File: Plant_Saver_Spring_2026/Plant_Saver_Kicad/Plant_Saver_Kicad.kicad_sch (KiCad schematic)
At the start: 27 parts, among them SW1 Up, SW2 Down, SW3 Change Screen, SW4 Select, U3 ESP32-WROOM-32D, U5 TPB4056A20-ES1R, U6 AMS1117-3.3

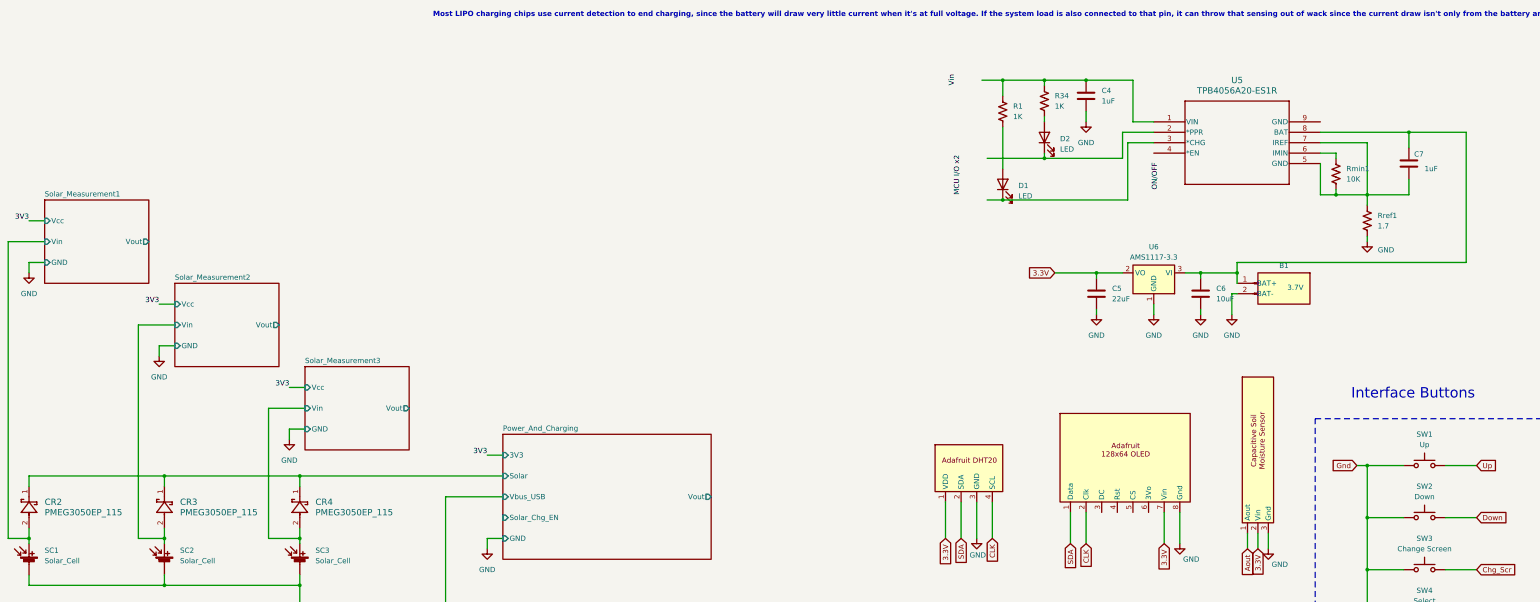
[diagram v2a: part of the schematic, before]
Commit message: Updated Charging Circuit
Replaced TP4056 with MCP73833, replaced schottky diodes
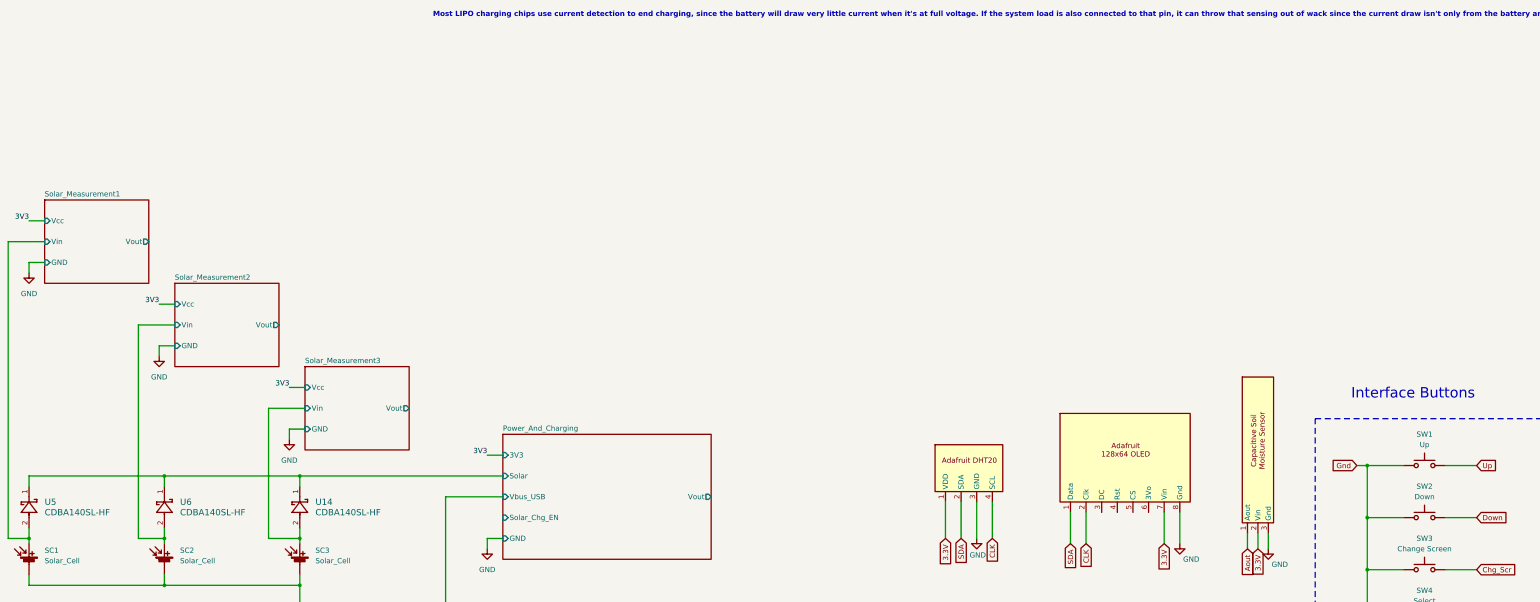
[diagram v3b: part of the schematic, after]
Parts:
- removed B1: 3.7V, Connector_JST:JST_GH_BM02B-GHS-TBT_1x02-1MP_P1.25mm_Vertical, symbol Connector:Conn_01x02_Pin
- removed C4, C7: 1uF, symbol Device:C
- removed C5: 22uF, symbol Device:C
- removed C6: 10uF, symbol Device:C
- removed CR2, CR3, CR4: PMEG3050EP_115, symbol PMEG3050EP,115:PMEG3050EP_115
- removed D1, D2: LED, symbol Device:LED
- removed R1, R34: 1K, symbol Device:R_US
- removed Rmin1: 10K, symbol Device:R_US
- removed Rref1: 1.7, symbol Device:R_US
- removed U5: TPB4056A20-ES1R, footprints:ESOP-8_TPK, symbol 2026-01-15_14-25-32:TPB4056A20-ES1R
- removed U6: AMS1117-3.3, Package_TO_SOT_SMD:SOT-223-3_TabPin2, symbol Regulator_Linear:AMS1117-3.3
- added U14, U5, U6: CDBA140SL-HF, CDBA-HF, symbol CDBA140SL_HF:CDBA140SL-HF
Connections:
- net Power_And_Charging/Solar: now also U14.1, U5.1, U6.1
- net Solar_Measurement1/Vin: now also U5.2
- net Solar_Measurement2/Vin: now also U6.2
- net Solar_Measurement3/Vin: now also U14.2

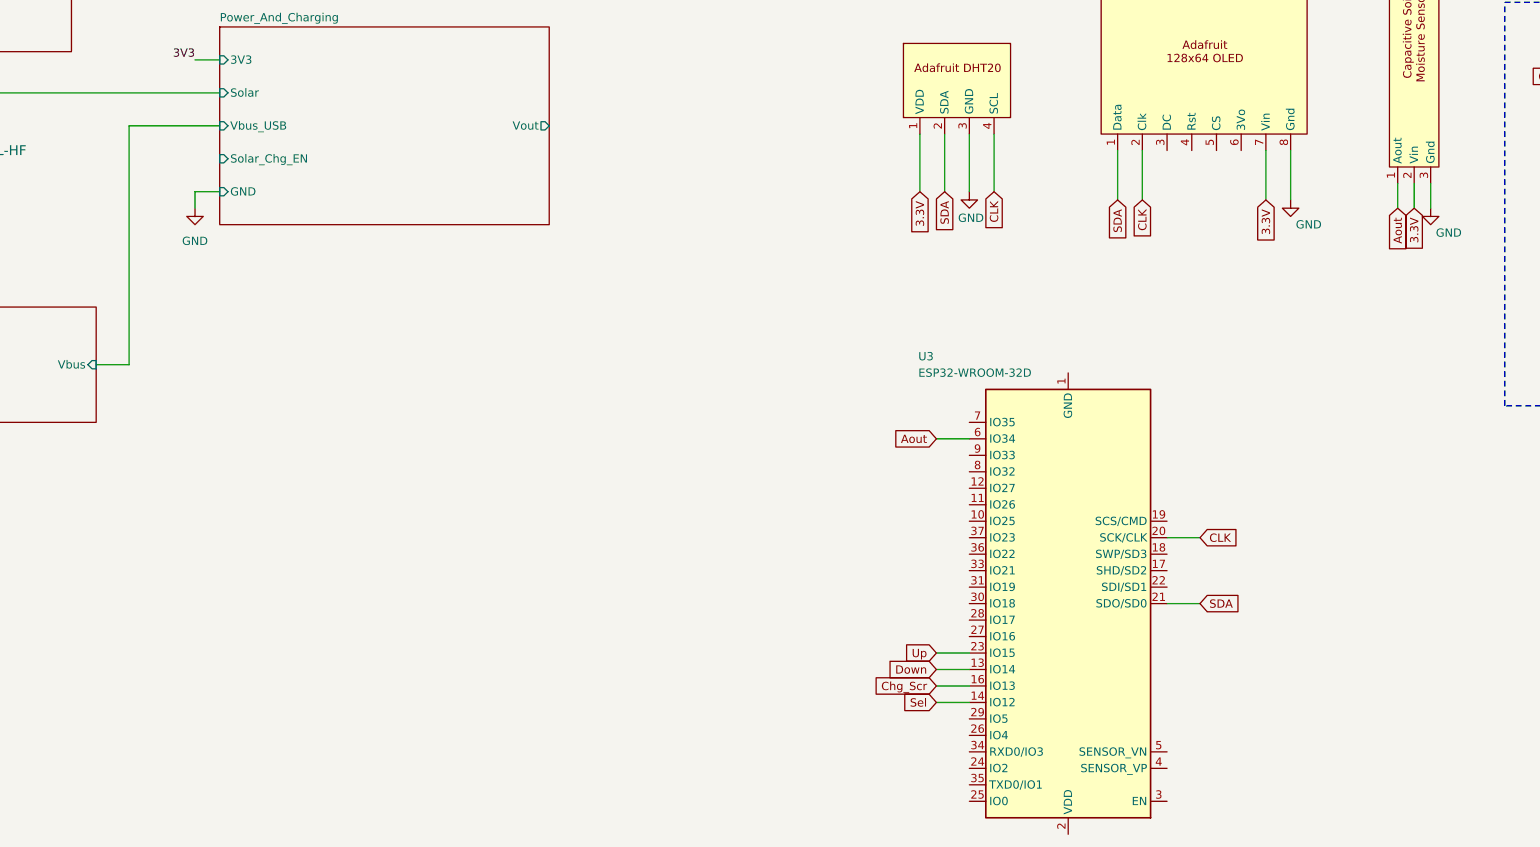
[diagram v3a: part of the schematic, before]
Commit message: Added ESP32 micro and mostly completed its wiring to peripherals
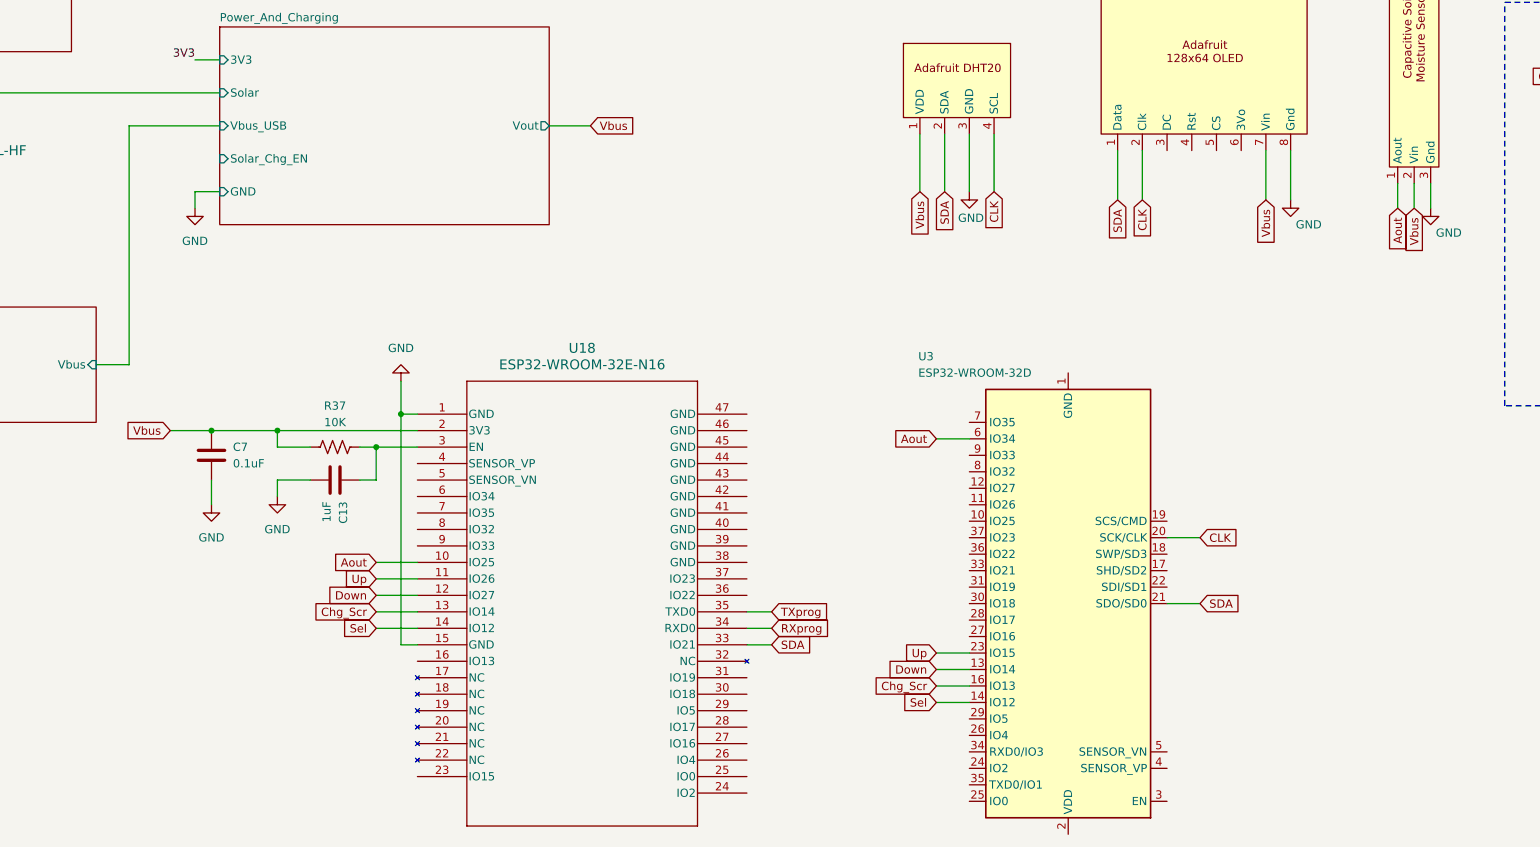
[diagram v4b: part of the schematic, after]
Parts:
- added C13: 1uF, Capacitor_THT:C_Disc_D4.7mm_W2.5mm_P5.00mm, symbol Device:C
- added C7: 0.1uF, Capacitor_THT:C_Disc_D4.7mm_W2.5mm_P5.00mm, symbol Device:C
- added R37: 10K, Resistor_THT:R_Axial_DIN0207_L6.3mm_D2.5mm_P10.16mm_Horizontal, symbol Device:R_US
- added U18: ESP32-WROOM-32E-N16, ul_ESP32-WROOM-32E-N16:ESP32­WROOM­32E_EXP, symbol ul_ESP32-WROOM-32E-N16:ESP32-WROOM-32E-N16
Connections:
- net Aout: now also U18.10 (IO25)
- net Chg_Scr: now also U18.13 (IO14)
- net Down: now also U18.12 (IO27)
- net GND: now also C13.2, C7.2, U18.1 (GND), U18.15 (GND)
- net SDA: now also U18.33 (IO21)
- net Sel: now also U18.14 (IO12)
- net Up: now also U18.11 (IO26)
- net 3.3V renamed Vbus
- net Vbus: now also C7.1, R37.1, U18.2 (3V3)
- new net: C13.1, R37.2, U18.3 (EN)
- new net RXprog: U18.34 (RXD0)
- new net TXprog: U18.35 (TXD0)

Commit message: minor microcontroller adjustments
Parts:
- added SW5: Select, symbol Switch:SW_Push
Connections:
- net CLK: now also U18.30 (IO18)
- net GND: now also SW5.2
- net at U18.25 (IO0): now also SW5.1
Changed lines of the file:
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@@
 	(wire
 		(pts
+			(xy 224.79 229.87) (xy 228.6 229.87)
+		)
+		(stroke
+			(width 0)
+			(type default)
+		)
+	)
+	(wire
+		(pts
 			(xy 142.24 189.23) (xy 152.4 189.23)
 		)
@@
 	(wire
 		(pts
+			(xy 224.79 242.57) (xy 228.6 242.57)
+		)
+		(stroke
+			(width 0)
+			(type default)
+		)
+	)
+	(wire
+		(pts
 			(xy 27.94 137.16) (xy 27.94 139.7)
 		)
@@
 	(wire
 		(pts
+			(xy 241.3 245.11) (xy 241.3 242.57)
+		)
+		(stroke
+			(width 0)
+			(type default)
+		)
+	)
+	(wire
+		(pts
 			(xy 31.75 85.09) (xy 27.94 85.09)
 		)
@@
 	(wire
 		(pts
+			(xy 241.3 242.57) (xy 238.76 242.57)
+		)
+		(stroke
+			(width 0)
+			(type default)
+		)
+	)
+	(wire
+		(pts
 			(xy 354.33 147.32) (xy 363.22 147.32)
 		)
@@
 		)
 	)
+	(global_label "CLK"
+		(shape input)
+		(at 228.6 229.87 0)
+		(fields_autoplaced yes)
+		(effects
+			(font
+				(size 1.27 1.27)
+			)
+			(justify left)
+		)
+		(property "Intersheetrefs" "${INTERSHEET_REFS}"
+			(at 235.1533 229.87 0)
+			(effects
+				(font
+					(size 1.27 1.27)
+				)
+				(justify left)
+				(hide yes)
+			)
+		)
+	)
 	(global_label "Sel"
 		(shape input)
@@
 	)
 	(symbol
+		(lib_id "Switch:SW_Push")
+		(at 233.68 242.57 0)
+		(unit 1)
+		(exclude_from_sim no)
+		(in_bom yes)
+		(on_board yes)
+		(dnp no)
+		(fields_autoplaced yes)
+		(property "Reference" "SW5"
+			(at 233.68 234.95 0)
+			(effects
+				(font
+					(size 1.27 1.27)
+				)
+			)
+		)
+		(property "Value" "Select"
+			(at 233.68 237.49 0)
+			(effects
+				(font
+					(size 1.27 1.27)
+				)
+			)
+		)
+		(property "Footprint" ""
+			(at 233.68 237.49 0)
+			(effects
+				(font
+					(size 1.27 1.27)
+				)
+				(hide yes)
+			)
+		)
+		(property "Datasheet" "~"
+			(at 233.68 237.49 0)
+			(effects
+				(font
+					(size 1.27 1.27)
+				)
+				(hide yes)
+			)
+		)
+		(property "Description" "Push button switch, generic, two pins"
+			(at 233.68 242.57 0)
+			(effects
+				(font
+					(size 1.27 1.27)
+				)
+				(hide yes)
+			)
+		)
+		(pin "2"
+		)
+		(pin "1"
+		)
+		(instances
+			(project "Plant_Saver_Kicad"
+				(path "/7f244634-d37a-4ff0-ba36-8027330ab1bd"
+					(reference "SW5")
+					(unit 1)
+				)
+			)
+		)
+	)
+	(symbol
 		(lib_id "Device:Solar_Cell")
 		(at 93.98 158.75 0)
@@
 					(unit 1)
 				)
+			)
+		)
+	)
+	(symbol
+		(lib_id "power:GND")
+		(at 241.3 245.11 0)
+		(unit 1)
+		(exclude_from_sim no)
+		(in_bom yes)
+		(on_board yes)
+		(dnp no)
+		(fields_autoplaced yes)
+		(property "Reference" "#PWR027"
+			(at 241.3 251.46 0)
+			(effects
+				(font
+					(size 1.27 1.27)
+				)
+				(hide yes)
+			)
+		)
+		(property "Value" "GND"
+			(at 241.3 250.19 0)
+			(effects
+				(font
+					(size 1.27 1.27)
+				)
+			)
+		)
+		(property "Footprint" ""
+			(at 241.3 245.11 0)
+			(effects
+				(font
+					(size 1.27 1.27)
+				)
+				(hide yes)
+			)
+		)
+		(property "Datasheet" ""
+			(at 241.3 245.11 0)
+			(effects
+				(font
+					(size 1.27 1.27)
+				)
+				(hide yes)
+			)
+		)
+		(property "Description" "Power symbol creates a global label with name \"GND\" , ground"
+			(at 241.3 245.11 0)
+			(effects
+				(font
+					(size 1.27 1.27)
+				)
+				(hide yes)
+			)
+		)
+		(pin "1"
+		)
+		(instances
+			(project "Plant_Saver_Kicad"
+				(path "/7f244634-d37a-4ff0-ba36-8027330ab1bd"
+					(reference "#PWR027")
+					(unit 1)
+				)

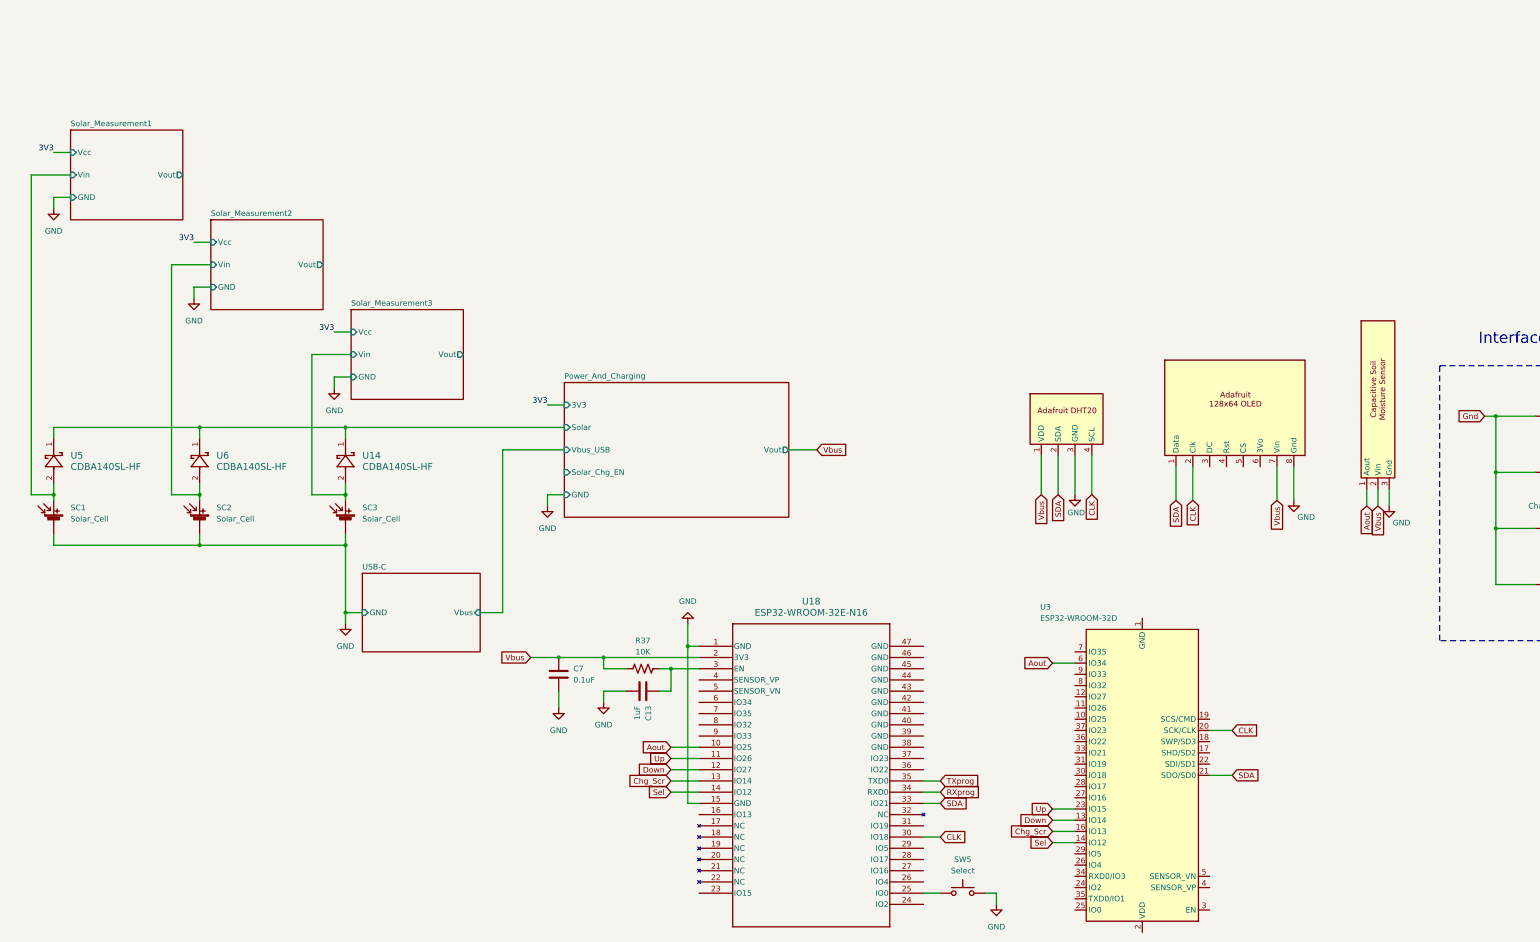
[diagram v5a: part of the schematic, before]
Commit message: Updates to power schematic
Replaced certain selection transistors for lower Rds_on, added thermal cutoff and DW03 for battery protection, swapped in 4-channel op-amps for solar measurement, various misc. improvements.
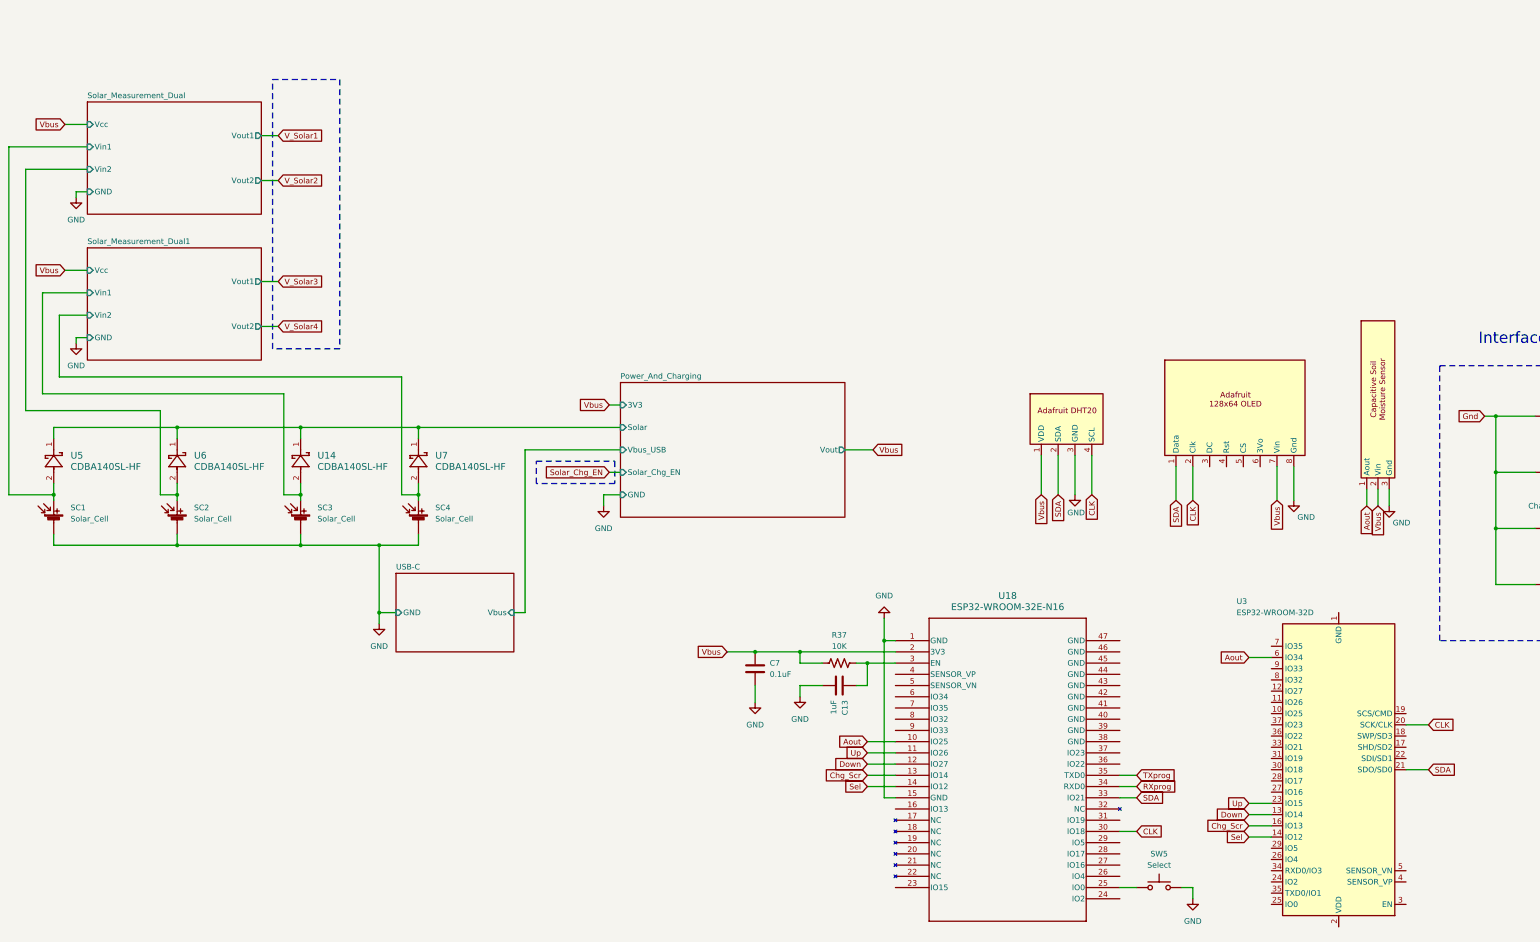
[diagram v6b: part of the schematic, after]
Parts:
- added SC4: Solar_Cell, symbol Device:Solar_Cell
- added U7: CDBA140SL-HF, CDBA-HF, symbol CDBA140SL_HF:CDBA140SL-HF
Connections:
- net GND: now also SC4.2 (-)
- net Power_And_Charging/Solar: now also U7.1
- net Solar_Measurement1/Vin renamed Solar_Measurement_Dual/Vin1
- net Solar_Measurement2/Vin renamed Solar_Measurement_Dual/Vin2
- net Solar_Measurement3/Vin renamed Solar_Measurement_Dual1/Vin1
- new net Solar_Measurement_Dual1/Vin2: SC4.1 (+), U7.2
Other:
- removed sheet Solar_Measurement1
- removed sheet Solar_Measurement2
- removed sheet Solar_Measurement3
- added sheet Solar_Measurement_Dual (Solar_Measurement_Dual.kicad_sch)
- added sheet Solar_Measurement_Dual1 (Solar_Measurement_Dual.kicad_sch)
- moved on the sheet: C13, C7, R37, SC2, SC3, SW5, U14, U18, U3, U6
